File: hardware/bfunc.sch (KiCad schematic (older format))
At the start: 2 parts, among them J10 Conn_01x20_Male, J9 Conn_01x20_Male

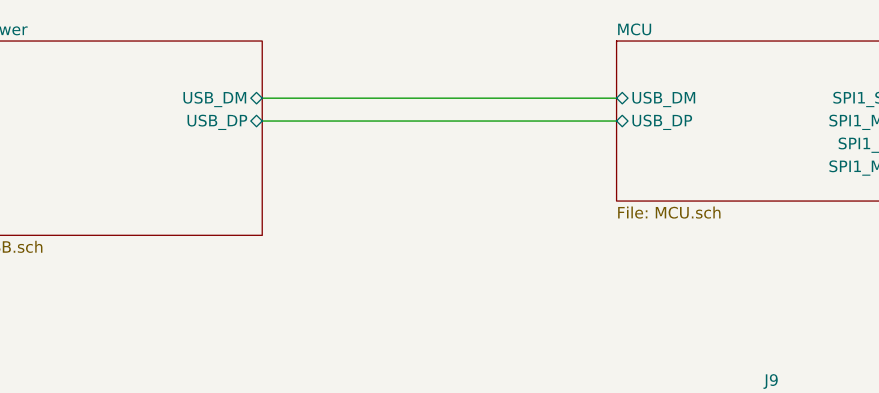
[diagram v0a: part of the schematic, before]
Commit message: Moved all Kicad stuff to /hardware/ directory
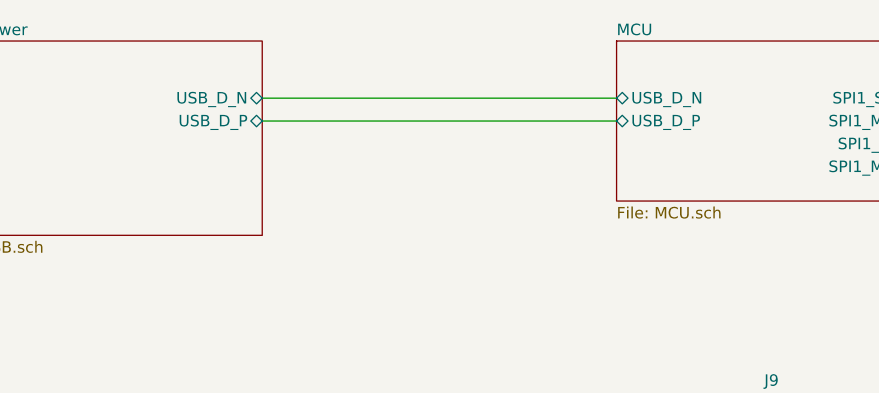
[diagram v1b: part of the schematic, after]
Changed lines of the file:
@@
 F0 "MCU" 50
 F1 "MCU.sch" 50
-F2 "USB_DM" B L 5000 3000 50
-F3 "USB_DP" B L 5000 3100 50
+F2 "USB_D_N" B L 5000 3000 50
+F3 "USB_D_P" B L 5000 3100 50
 F4 "SPI1_SS_L" O R 6350 3000 50
 F5 "SPI1_SCK" O R 6350 3200 50
@@
 F0 "USB/Power" 50
 F1 "USB.sch" 50
-F2 "USB_DP" B R 3450 3100 50
-F3 "USB_DM" B R 3450 3000 50
+F2 "USB_D_P" B R 3450 3100 50
+F3 "USB_D_N" B R 3450 3000 50
 $EndSheet
 Wire Wire Line
